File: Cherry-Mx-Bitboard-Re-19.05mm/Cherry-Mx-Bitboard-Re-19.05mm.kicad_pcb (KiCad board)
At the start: 2 copper layers, 17.8 x 17.8 mm, 11 parts, among them SW1 SW_Push

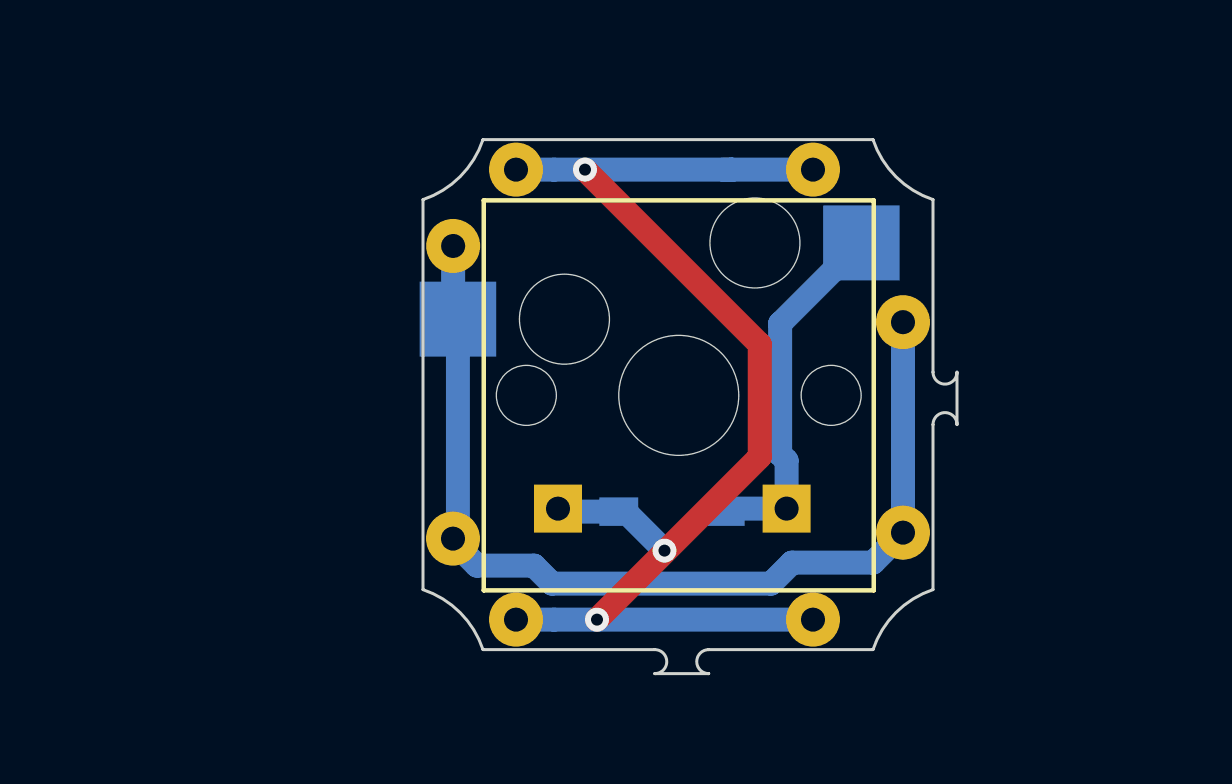
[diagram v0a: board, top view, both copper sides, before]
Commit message: added choc
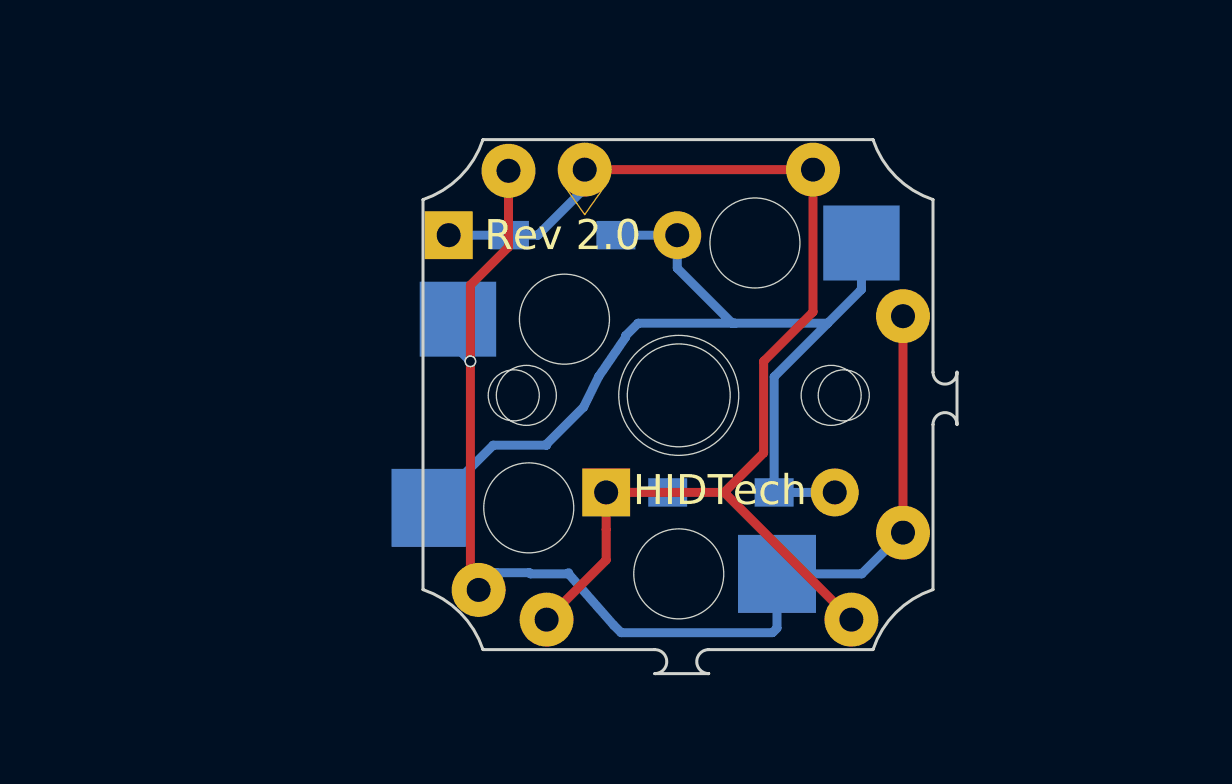
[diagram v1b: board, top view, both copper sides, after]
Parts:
- added D1: 1N4148W, Footprints:1N4148W, B.Cu at (85.0, 48.5)
- added D2: 1N4148W, Footprints:1N4148W, B.Cu at (88.8, 48.5)
- added SW2: SW_Push-Switch, keyswitches:Kailh_socket_PG1350, F.Cu at (92.7, 53.8)
- moved Row111 3.11 mm to (87.0, 46.4)
- moved Col111 2.29 mm to (89.5, 46.3)
- moved D2 1.75 mm to (94.1, 57.1)
- moved D1 1.69 mm to (90.2, 57.1)
- moved Col114 1.28 mm to (98.4, 61.3)
- moved Col113 1.02 mm to (88.3, 61.3)
- moved Row112 0.90 mm to (85.7, 59.3)
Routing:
- net Net-(D1-Pad2): track 12.2 -> 34.7 mm
- net Row1: track 34.9 -> 43.3 mm, vias 0 -> 1
- net Col1: track 44.5 -> 42.4 mm, vias 3 -> 0
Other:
- net class Default: clearance 0.3 -> 0.1; trace_width 0.8 -> 0.3; via_dia 0.8 -> 0.4; via_drill 0.4 -> 0.3
- rule trace_clearance: 0.3 -> 0.1
- board text added: "<Col->"
- board text added: "<Row>"
- board text added: "<—-Col->"
- board text added: "HIDTech"
- board text added: "Rev 2.0"
- board text removed: "Col"
- board text removed: "ProtoCases.com"
- board text removed: "v1.1"

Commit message: add rgb leds
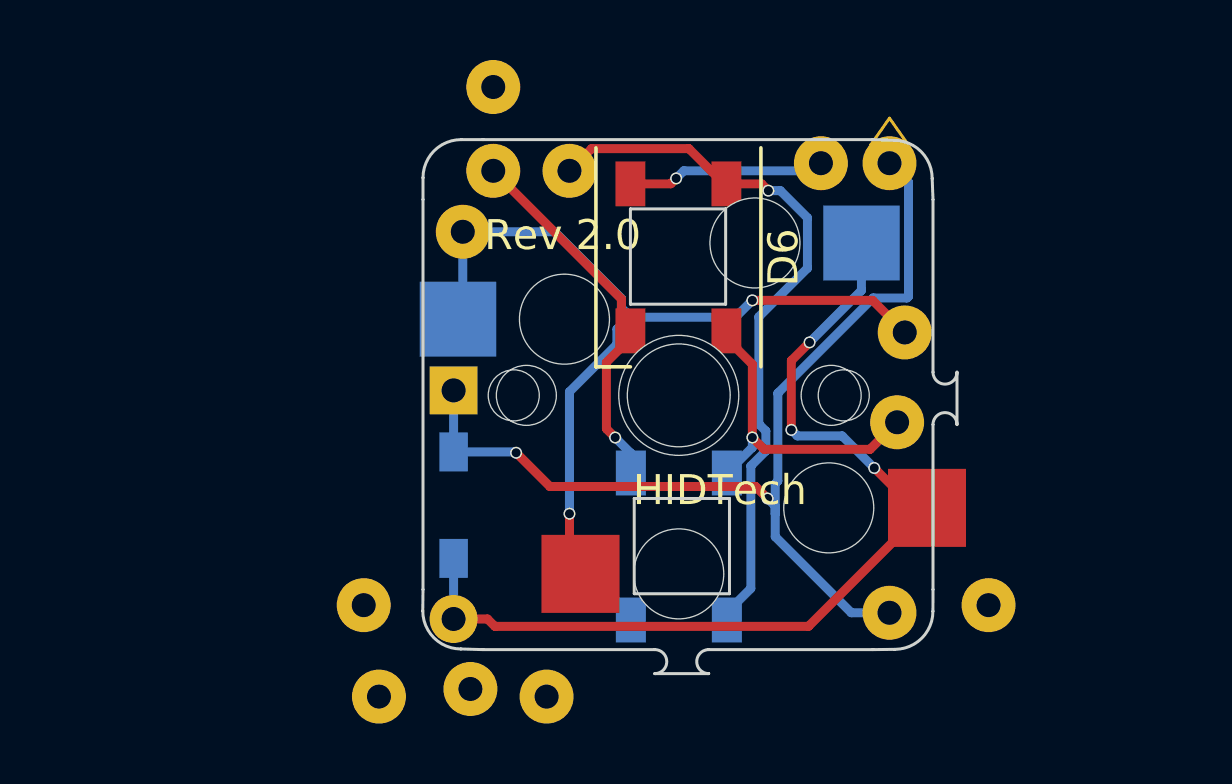
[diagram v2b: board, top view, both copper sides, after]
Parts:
- removed the D1 at (85.0, 48.5)
- removed the D1 at (90.2, 57.1)
- removed the D2 at (88.8, 48.5)
- removed the D2 at (94.1, 57.1)
- added D1: 1N4148W, Footprints:1N4148W, B.Cu at (85.2, 53.7)
- added D2: 1N4148W, Footprints:1N4148W, B.Cu at (85.2, 57.5)
- added D5: SK6812, LED_SMD:LED_SK6812_PLCC4_5.0x5.0mm_P3.2mm, B.Cu at (92.7, 58.9)
- added D6: SK6812, LED_SMD:LED_SK6812_PLCC4_5.0x5.0mm_P3.2mm, F.Cu at (92.7, 49.2)
- added Din1: Conn_01x01, Footprints:Wirepad, F.Cu at (99.9, 54.7)
- added Dout1: Conn_01x01, Footprints:Wirepad, F.Cu at (97.4, 46.1)
- added GND1: Conn_01x01, Footprints:Wirepad, F.Cu at (86.5, 46.4)
- added GND2: Conn_01x01, Footprints:Wirepad, F.Cu at (85.7, 63.6)
- added Vcc1: Conn_01x01, Footprints:Wirepad, F.Cu at (89.0, 46.4)
- added Vcc2: Conn_01x01, Footprints:Wirepad, F.Cu at (88.3, 63.9)
- Col112, Col113, Row112, Row114: moved to F.Cu
- SW2: moved to B.Cu
- moved Row114 18.1 mm to (82.2, 60.8)
- moved Row112 17.3 mm to (103.0, 60.8)
- moved Col112 11.0 mm to (86.5, 43.6)
- moved Col111 10.2 mm to (99.7, 46.1), turned to 180 degrees
- moved Col113 6.15 mm to (82.7, 63.9)
- moved Row111 2.54 mm to (85.5, 48.4)
- moved Col114 1.29 mm to (99.7, 61.1)
- moved Row113 0.55 mm to (100.2, 51.9)
- turned SW2 to 180 degrees
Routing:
- net VCC: track 0.00 -> 23.9 mm, vias 0 -> 1
- net GND: track 0.00 -> 12.6 mm, vias 0 -> 1
- net Row1: track 43.3 -> 32.1 mm, vias 1 -> 2
- net Din: track 0.00 -> 10.8 mm, vias 0 -> 1
- net Col1: track 42.4 -> 33.8 mm, vias 0 -> 2
- net Dout: track 0.00 -> 6.63 mm, vias 0 -> 1
- net Net-(D1-Pad2): track 34.7 -> 33.5 mm, vias 0 -> 3
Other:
- outline, holes or cut-outs redrawn
- board text removed: "<Col->"
- board text removed: "<Row>"
- board text removed: "<—-Col->"
- board text removed: "Row"

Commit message: simplified
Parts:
- moved Col114 30.8 mm to (72.8, 46.1)
- moved Row114 26.8 mm to (104.6, 46.1)
- moved Col111 23.4 mm to (76.3, 46.0)
- moved GND2 16.9 mm to (100.3, 55.1)
- moved Row113 16.2 mm to (85.0, 46.4)
- moved Row112 15.7 mm to (108.3, 46.1)
- moved Din1 15.0 mm to (85.0, 53.7)
- moved Row111 14.9 mm to (100.2, 46.2)
- moved Vcc1 13.2 mm to (100.3, 53.2)
- moved GND1 11.3 mm to (85.0, 57.6)
- moved Vcc2 8.89 mm to (85.0, 55.6)
- moved D1 7.69 mm to (85.1, 61.4), turned to 57.5 degrees
- moved Dout1 5.87 mm to (100.3, 51.2)
- moved Col113 4.90 mm to (86.9, 61.5)
- moved Col112 2.65 mm to (87.0, 46.2)
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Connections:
- SW1 pad 1: Row1 -> Net-(D1-Pad2)
- SW1 pad 2: Net-(D1-Pad2) -> Row1
- SW2 pad 1: Row1 -> Net-(D1-Pad2)
- SW2 pad 2: Net-(D1-Pad2) -> Row1
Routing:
- net Col1: track 33.8 -> 0.14 mm, vias 2 -> 0
- net Row1: track 32.1 -> 0.00 mm, vias 2 -> 0
- net Net-(D1-Pad2): track 33.5 -> 1.98 mm, vias 3 -> 0
- net VCC: track 23.9 -> 0.00 mm, vias 1 -> 0
- net GND: track 12.6 -> 0.00 mm, vias 1 -> 0
- net Din: track 10.8 -> 0.00 mm, vias 1 -> 0
- net Dout: track 6.63 -> 0.25 mm, vias 1 -> 0
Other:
- outline, holes or cut-outs redrawn

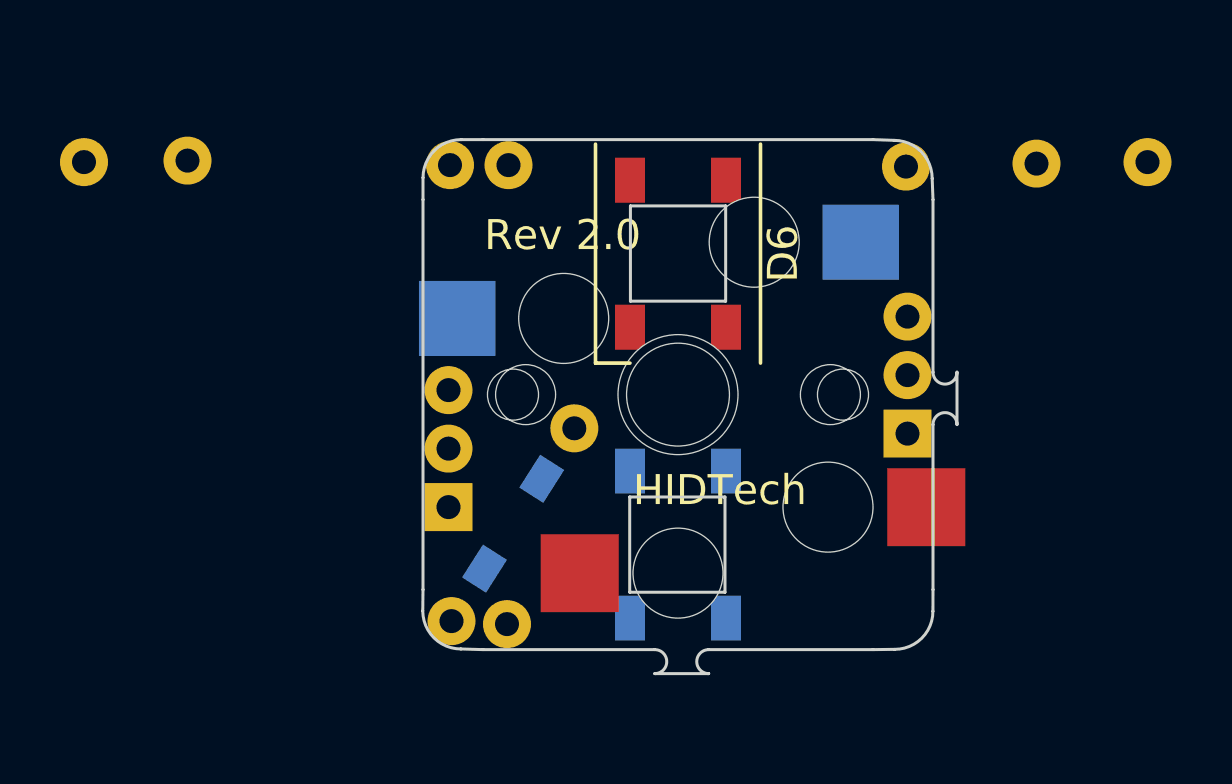
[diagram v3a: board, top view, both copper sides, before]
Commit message: fix both sides rgb leds
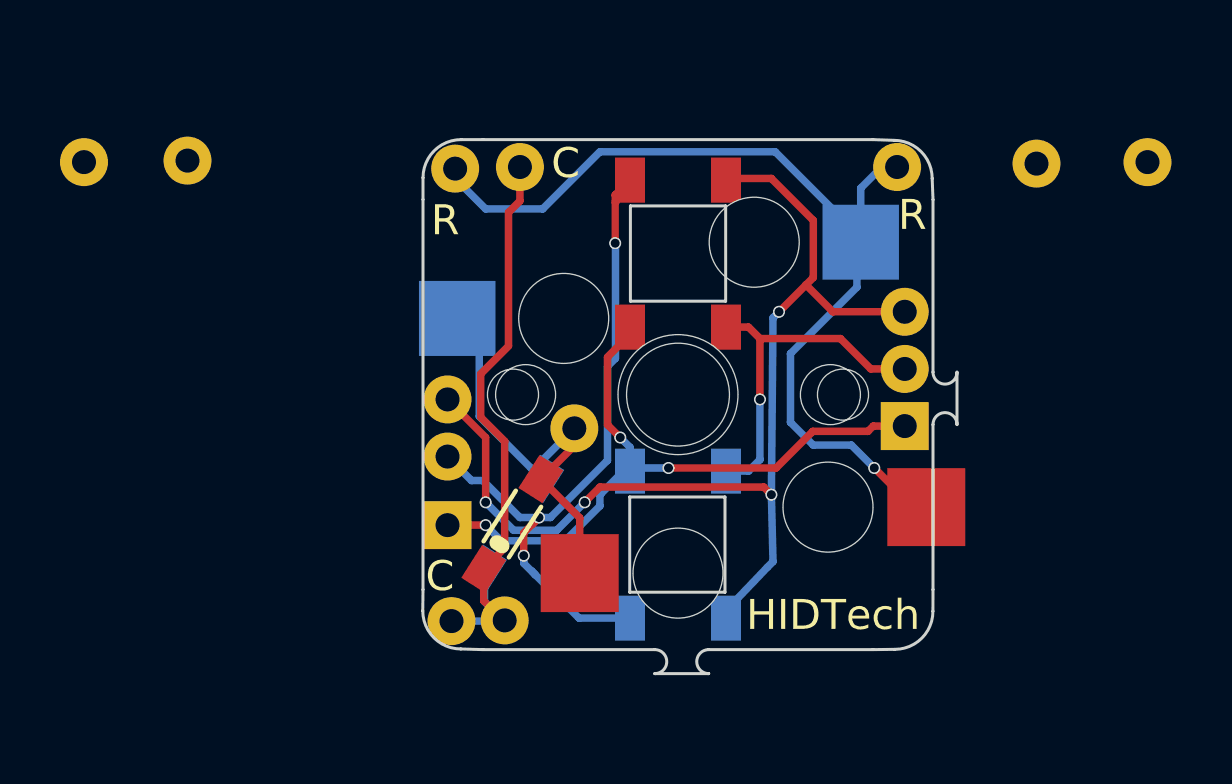
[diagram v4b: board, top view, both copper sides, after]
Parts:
- added D3: 1N4148W, Footprints:1N4148W, F.Cu at (87.1, 58.1)
- moved Dout1 16.0 mm to (85.0, 55.9)
- moved Din1 15.2 mm to (100.2, 53.0)
- moved Vcc1 2.11 mm to (100.2, 51.1)
- moved Vcc2 1.64 mm to (85.0, 54.0)
- moved GND1 0.60 mm to (85.0, 58.2)
- moved Col112 0.39 mm to (87.4, 46.2)
- moved Row111 0.30 mm to (99.9, 46.2)
- moved GND2 0.27 mm to (100.2, 54.9)
- moved Row113 0.21 mm to (85.2, 46.5)
- moved Col113 0.15 mm to (86.9, 61.3)
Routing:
- net VCC: track 0.00 -> 36.6 mm, vias 0 -> 4
- net Row1: track 0.00 -> 33.6 mm, vias 0 -> 1
- net Dout: track 0.25 -> 25.1 mm, vias 0 -> 3
- net GND: track 0.00 -> 24.6 mm, vias 0 -> 3
- net Col1: track 0.14 -> 20.8 mm
- net Net-(D1-Pad2): track 1.98 -> 17.6 mm
- net Din: track 0.00 -> 11.9 mm, vias 0 -> 1
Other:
- net class Default: trace_width 0.3 -> 0.25
- board text added: "C"
- board text added: "R"
